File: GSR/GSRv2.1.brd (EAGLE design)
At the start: 67.3 x 52.1 mm, 38 parts, among them U1 ARDUINO_MINI

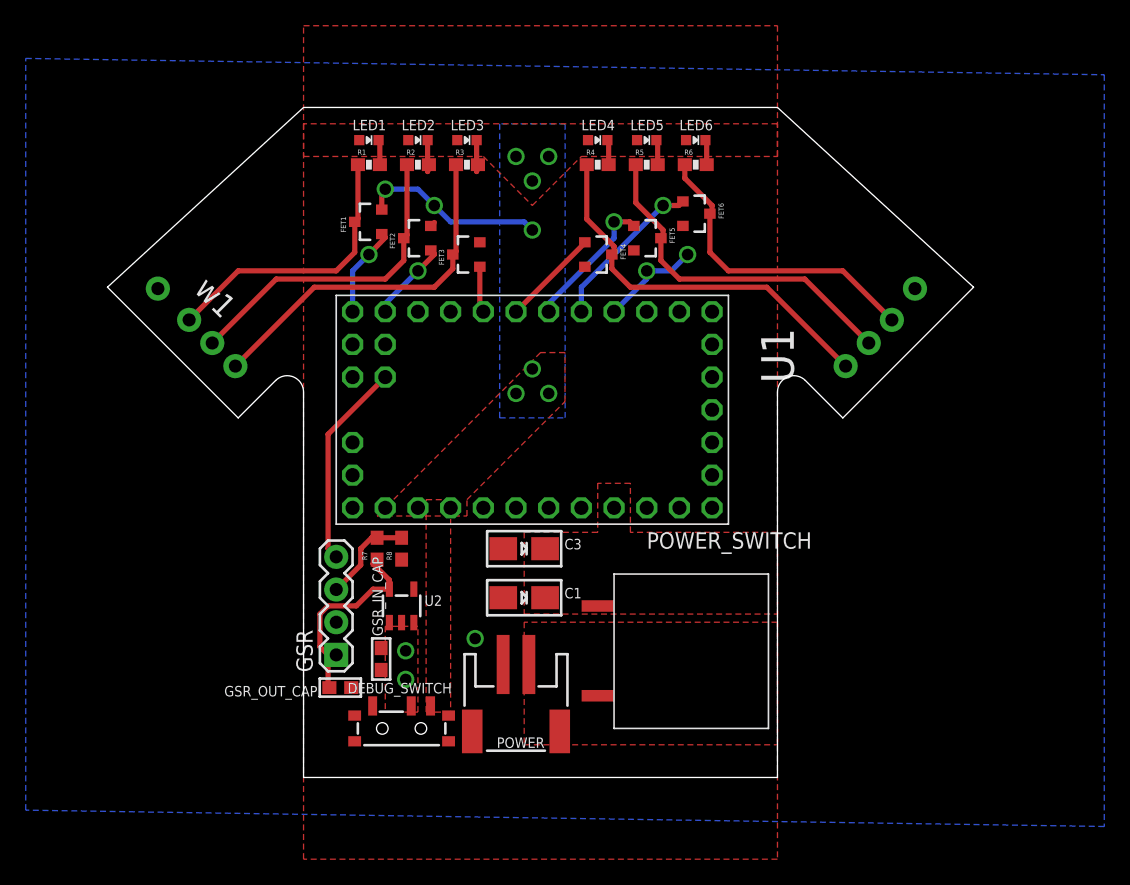
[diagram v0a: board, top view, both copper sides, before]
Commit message: fixed errors and aligned board
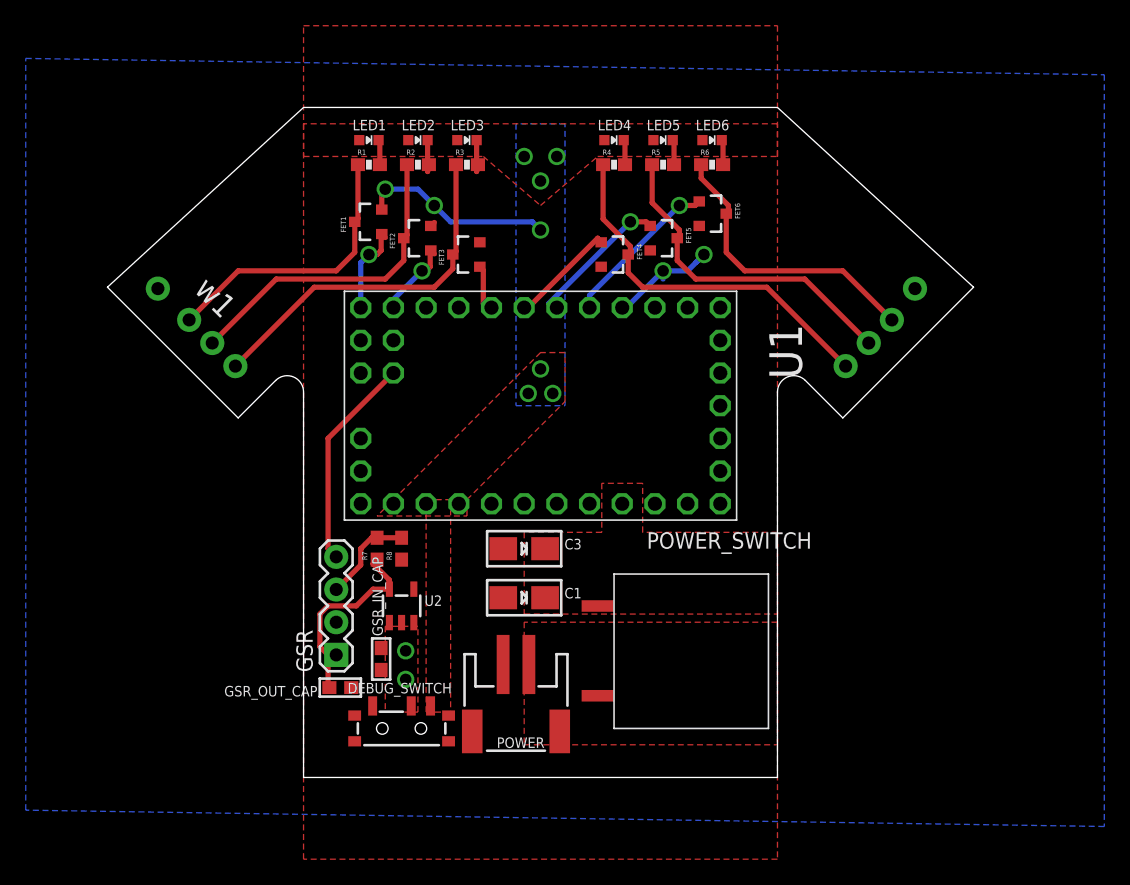
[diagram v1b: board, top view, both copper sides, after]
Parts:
- moved FET4 1.27 mm to (47.0, 38.1)
- moved LED4 1.27 mm to (47.0, 47.0)
- moved R4 1.27 mm to (47.0, 45.1)
- moved FET5 1.27 mm to (50.8, 39.4)
- moved FET6 1.27 mm to (54.6, 41.3)
- moved LED5 1.27 mm to (50.8, 47.0)
- moved LED6 1.27 mm to (54.6, 47.0)
- moved R5 1.27 mm to (50.8, 45.1)
- moved R6 1.27 mm to (54.6, 45.1)
- moved U1 0.71 mm to (40.0, 26.4)
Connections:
- removed net N$7: POWER.2
- net GND: now also POWER.2
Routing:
- net GND: track 22.8 -> 25.1 mm, vias 6 -> 5
- net WIRE6: track 24.1 -> 22.8 mm
- net WIRE5: track 27.2 -> 25.9 mm
- net WIRE4: track 30.3 -> 29.3 mm
- net FET4: track 7.61 -> 8.43 mm
- net FET5: track 10.8 -> 11.4 mm
- net GSR_SIG: track 16.1 -> 16.7 mm

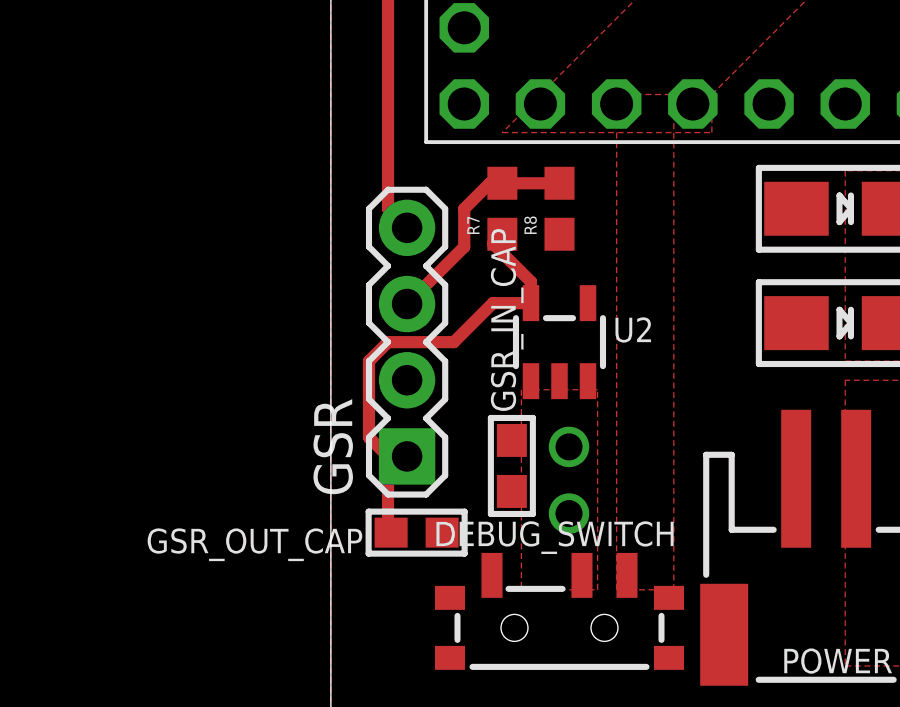
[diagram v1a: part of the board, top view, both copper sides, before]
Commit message: reduced the width of a route to fix clearance issues. found unrouted wire.
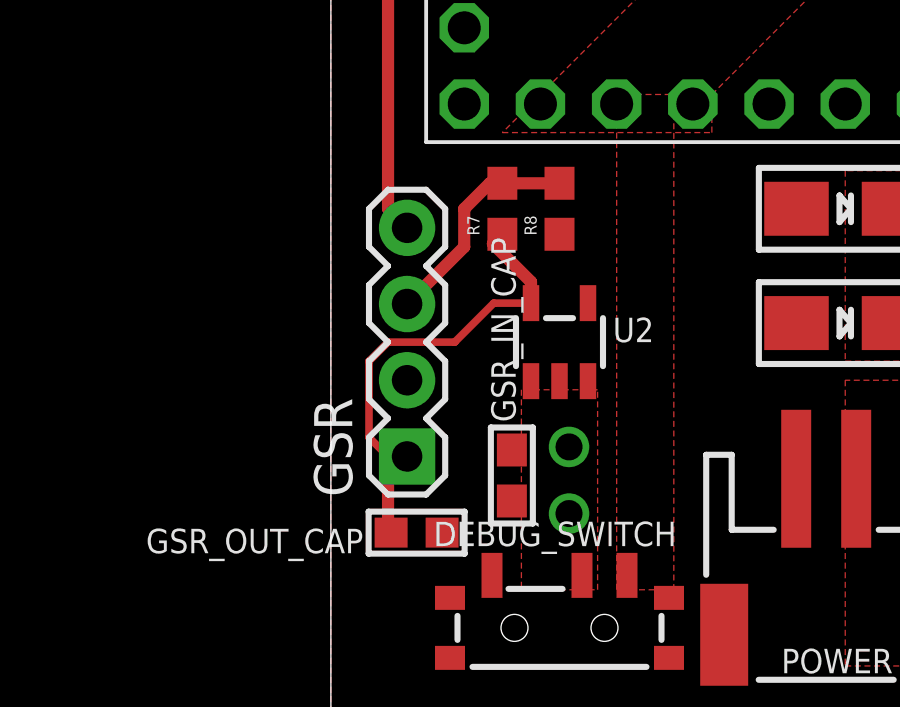
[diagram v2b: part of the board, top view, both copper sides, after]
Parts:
- moved GSR_IN_CAP 0.32 mm to (28.9, 6.35)
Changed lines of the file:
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@@
 <element name="DEBUG_SWITCH" library="microbuilder" package="SPST_SMT_19192" value="" x="30.48" y="1.27"/>
 <element name="GSR_OUT_CAP" library="microbuilder" package="0603" value="1uF" x="25.7175" y="4.445" rot="R180"/>
-<element name="GSR_IN_CAP" library="microbuilder" package="0603" value="1uF" x="28.8925" y="6.6675" rot="R90"/>
+<element name="GSR_IN_CAP" library="microbuilder" package="0603" value="1uF" x="28.8925" y="6.35" rot="R90"/>
 </elements>
 <signals>
@@
 <vertex x="31.75" y="2.54"/>
 </polygon>
-<wire x1="31.43" y1="9.4949" x2="29.53" y2="9.4949" width="0" layer="19" extent="1-1"/>
 </signal>
 <signal name="VIN">
@@
 <wire x1="28.26" y1="14.075" x2="29.53" y2="12.805" width="0.4064" layer="1"/>
 <wire x1="29.53" y1="12.805" x2="29.53" y2="12.0951" width="0.4064" layer="1"/>
-<wire x1="25.4" y1="6.985" x2="24.765" y2="6.985" width="0.4064" layer="1"/>
-<wire x1="24.765" y1="6.985" x2="24.13" y2="7.62" width="0.4064" layer="1"/>
-<wire x1="24.13" y1="7.62" x2="24.13" y2="10.16" width="0.4064" layer="1"/>
-<wire x1="24.13" y1="10.16" x2="24.765" y2="10.795" width="0.4064" layer="1"/>
-<wire x1="24.765" y1="10.795" x2="26.9599" y2="10.795" width="0.4064" layer="1"/>
 <contactref element="GSR_OUT_CAP" pad="2"/>
-<wire x1="29.53" y1="12.0951" x2="28.26" y2="12.0951" width="0.4064" layer="1"/>
-<wire x1="28.26" y1="12.0951" x2="26.9599" y2="10.795" width="0.4064" layer="1"/>
 <wire x1="24.765" y1="6.985" x2="24.765" y2="4.5475" width="0.4064" layer="1"/>
 <wire x1="24.765" y1="4.5475" x2="24.8675" y2="4.445" width="0.4064" layer="1"/>
+<wire x1="29.53" y1="12.0951" x2="28.2876" y2="12.0951" width="0.254" layer="1"/>
+<wire x1="28.2876" y1="12.0951" x2="26.9875" y2="10.795" width="0.254" layer="1"/>
+<wire x1="26.9875" y1="10.795" x2="24.765" y2="10.795" width="0.254" layer="1"/>
+<wire x1="24.765" y1="10.795" x2="24.13" y2="10.16" width="0.254" layer="1"/>
+<wire x1="24.13" y1="10.16" x2="24.13" y2="7.62" width="0.254" layer="1"/>
+<wire x1="24.13" y1="7.62" x2="24.765" y2="6.985" width="0.254" layer="1"/>
+<wire x1="24.765" y1="6.985" x2="25.4" y2="6.985" width="0.254" layer="1"/>
 </signal>
 <signal name="GSR_SIG">

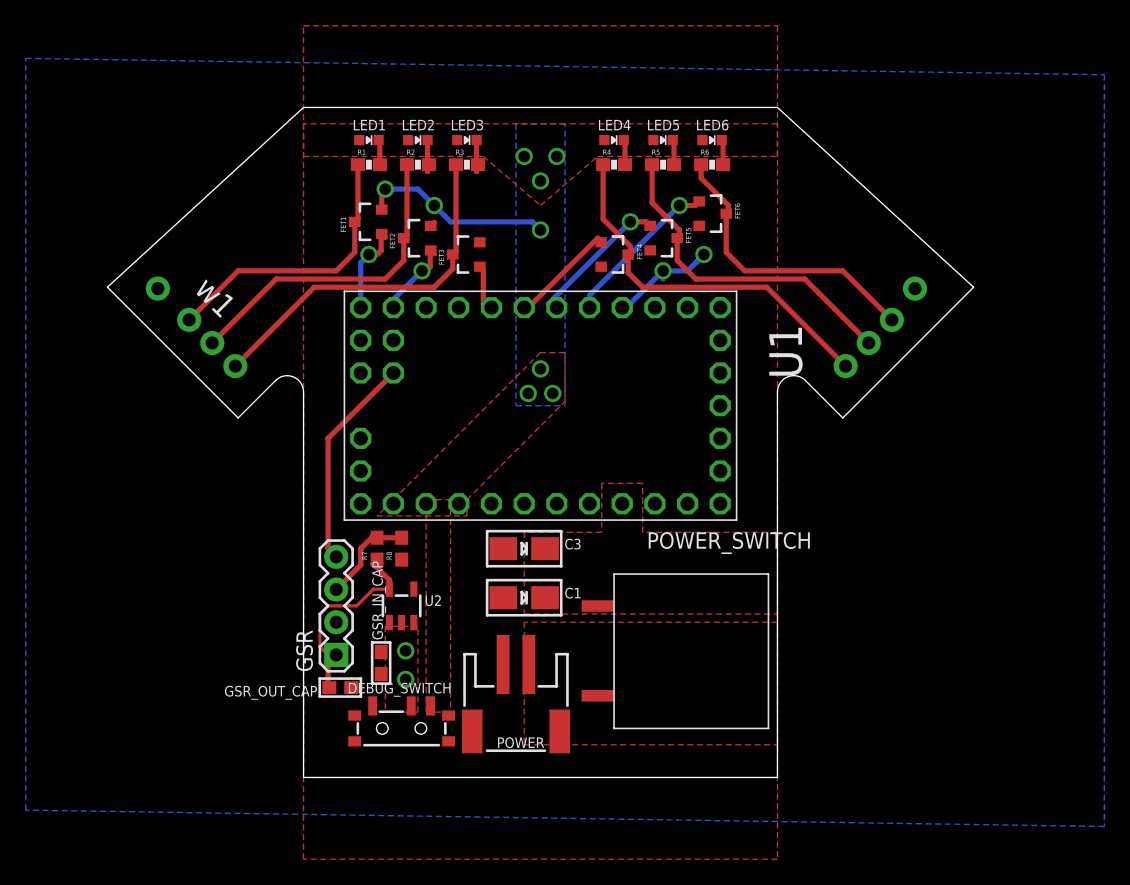
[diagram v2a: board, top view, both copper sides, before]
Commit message: added vias for vbat
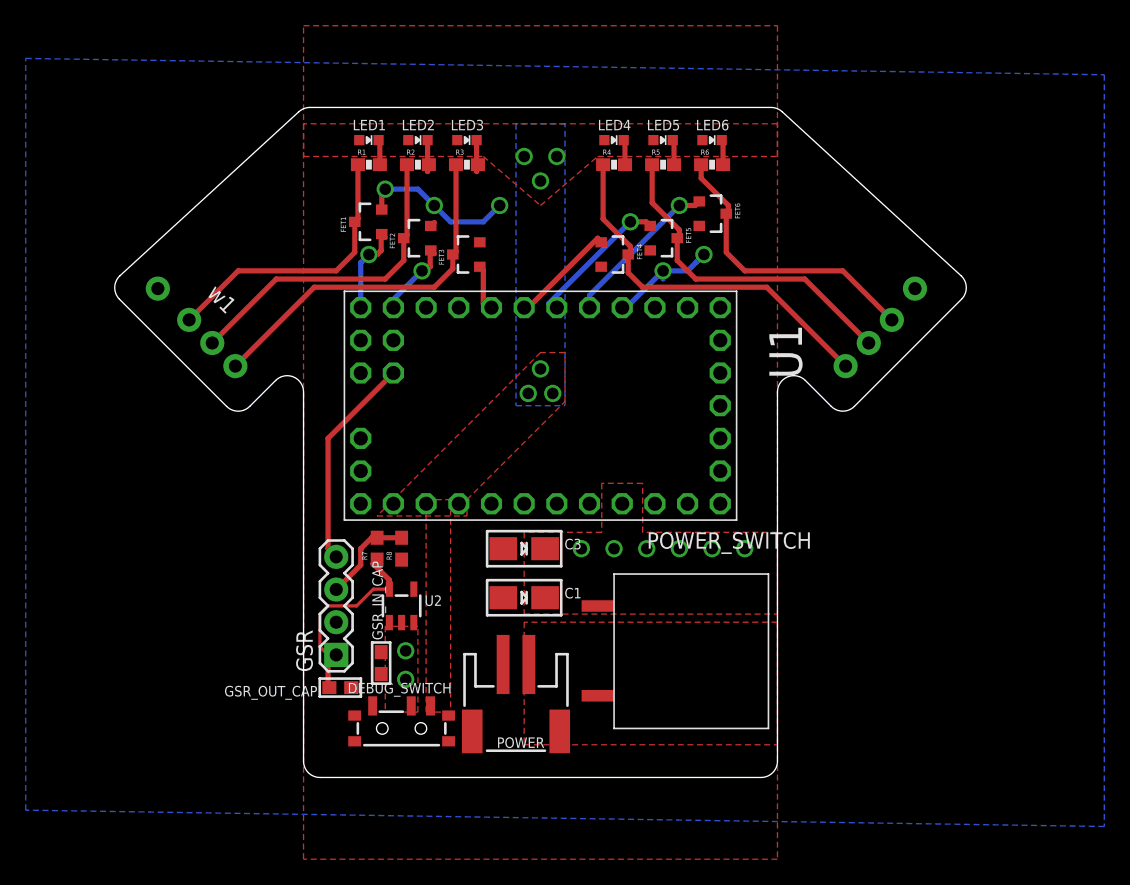
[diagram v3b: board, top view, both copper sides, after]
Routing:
- net GND: track 25.1 -> 22.1 mm
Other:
- board size 67.3 x 52.1 mm -> 66.2 x 52.1 mm
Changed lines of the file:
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@@
 <board>
 <plain>
-<wire x1="17.78" y1="25.4" x2="20.691975" y2="28.311975" width="0" layer="20"/>
+<wire x1="8.597775" y1="36.45629375" x2="22.4958375" y2="49.196184375" width="0" layer="20"/>
+<wire x1="22.4958375" y1="49.196184375" x2="23.354009375" y2="49.53" width="0" layer="20" curve="-42.510579"/>
+<wire x1="73.99208125" y1="34.62208125" x2="65.668025" y2="26.298025" width="0" layer="20"/>
+<wire x1="65.668025" y1="26.298025" x2="63.871975" y2="26.298025" width="0" layer="20" curve="-90"/>
+<wire x1="63.871975" y1="26.298025" x2="61.858025" y2="28.311975" width="0" layer="20"/>
+<wire x1="73.99208125" y1="34.62208125" x2="73.952225" y2="36.45629375" width="0" layer="20" curve="92.489657"/>
+<wire x1="73.952225" y1="36.45629375" x2="60.0541625" y2="49.196184375" width="0" layer="20"/>
+<wire x1="60.0541625" y1="49.196184375" x2="59.195990625" y2="49.53" width="0" layer="20" curve="42.510579"/>
+<wire x1="59.195990625" y1="49.53" x2="23.354009375" y2="49.53" width="0" layer="20"/>
+<wire x1="8.597775" y1="36.45629375" x2="8.55791875" y2="34.62208125" width="0" layer="20" curve="92.489661"/>
+<wire x1="8.55791875" y1="34.62208125" x2="16.881975" y2="26.298025" width="0" layer="20"/>
+<wire x1="16.881975" y1="26.298025" x2="18.678025" y2="26.298025" width="0" layer="20" curve="90"/>
+<wire x1="18.678025" y1="26.298025" x2="20.691975" y2="28.311975" width="0" layer="20"/>
 <wire x1="20.691975" y1="28.311975" x2="22.86" y2="27.41395" width="0" layer="20" curve="-135"/>
-<wire x1="22.86" y1="27.41395" x2="22.86" y2="-2.54" width="0" layer="20"/>
-<wire x1="22.86" y1="49.53" x2="7.62" y2="35.56" width="0" layer="20"/>
-<wire x1="64.77" y1="25.4" x2="61.858025" y2="28.311975" width="0" layer="20"/>
+<wire x1="58.42" y1="-2.54" x2="24.13" y2="-2.54" width="0" layer="20"/>
+<wire x1="24.13" y1="-2.54" x2="22.86" y2="-1.27" width="0" layer="20" curve="-90"/>
+<wire x1="22.86" y1="-1.27" x2="22.86" y2="27.41395" width="0" layer="20"/>
 <wire x1="61.858025" y1="28.311975" x2="59.69" y2="27.41395" width="0" layer="20" curve="135"/>
-<wire x1="59.69" y1="27.41395" x2="59.69" y2="-2.54" width="0" layer="20"/>
-<wire x1="64.77" y1="25.4" x2="74.93" y2="35.56" width="0" layer="20"/>
-<wire x1="74.93" y1="35.56" x2="59.69" y2="49.53" width="0" layer="20"/>
-<wire x1="22.86" y1="49.53" x2="59.69" y2="49.53" width="0" layer="20"/>
-<wire x1="59.69" y1="-2.54" x2="22.86" y2="-2.54" width="0" layer="20"/>
-<wire x1="7.62" y1="35.56" x2="17.78" y2="25.4" width="0" layer="20"/>
-<text x="17.78" y="34.29" size="1.778" layer="112" rot="R135">w1</text>
+<wire x1="59.69" y1="27.41395" x2="59.69" y2="-1.27" width="0" layer="20"/>
+<wire x1="59.69" y1="-1.27" x2="58.42" y2="-2.54" width="0" layer="20" curve="-90"/>
+<text x="17.78" y="34.29" size="1.27" layer="112" rot="R135">w1</text>
 </plain>
 <attributes>
@@
 <wire x1="29.21" y1="43.18" x2="31.75" y2="43.18" width="0.4064" layer="16"/>
 <wire x1="31.75" y1="43.18" x2="33.02" y2="41.91" width="0.4064" layer="16"/>
-<via x="41.275" y="40.005" extent="1-16" drill="0.9" shape="octagon"/>
+<via x="38.1" y="41.91" extent="1-16" drill="0.9" shape="octagon"/>
 <wire x1="32.75" y1="40.32" x2="33.02" y2="40.59" width="0.4064" layer="1"/>
 <via x="33.02" y="41.91" extent="1-16" drill="0.9" shape="octagon"/>
 <wire x1="33.02" y1="41.91" x2="34.29" y2="40.64" width="0.4064" layer="16"/>
-<wire x1="34.29" y1="40.64" x2="40.64" y2="40.64" width="0.4064" layer="16"/>
-<wire x1="40.64" y1="40.64" x2="41.275" y2="40.005" width="0.4064" layer="16"/>
+<wire x1="34.29" y1="40.64" x2="36.83" y2="40.64" width="0.4064" layer="16"/>
+<wire x1="36.83" y1="40.64" x2="38.1" y2="41.91" width="0.4064" layer="16"/>
 <contactref element="U2" pad="2"/>
 <contactref element="R8" pad="1"/>
@@
 <vertex x="31.75" y="2.54"/>
 </polygon>
+<via x="49.53" y="15.24" extent="1-16" drill="0.9"/>
+<via x="46.99" y="15.24" extent="1-16" drill="0.9"/>
+<via x="44.45" y="15.24" extent="1-16" drill="0.9"/>
+<via x="52.07" y="15.24" extent="1-16" drill="0.9"/>
+<via x="54.61" y="15.24" extent="1-16" drill="0.9"/>
+<via x="57.15" y="15.24" extent="1-16" drill="0.9"/>
 </signal>
 <signal name="VIN">
